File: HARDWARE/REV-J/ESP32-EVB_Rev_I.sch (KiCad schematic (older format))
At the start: 155 parts, among them CON1 TB3 DG306-5.0-3P, CON2 TB3 DG306-5.0-3P, Q1 BC817-40(SOT23), Q2 BC817-40(SOT23), Q3 Q12MHz/20pF/30ppm/2P/HC-49SM(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, Q4 BC817-40(SOT23), Q5 BC817-40(SOT23), Q6 BC817, Q7 BC817-40(SOT23), U1 BL4054B-42TPRN(SOT23-5), U10 BAT54C(SOT23-3), U2 SY8089AAAC(SOT23-5), U3 ESP-WROOM-32, U4 LAN8710A-EZC(QFN32), U5 CH340T(SSOP20W), U6 MCP2562-E/SN(SOIC-8_150mil), U7 RPM7236-H8, U8 NCP303LSN27T1G(SOT-23-5), U9 BAT54C(SOT23-3)

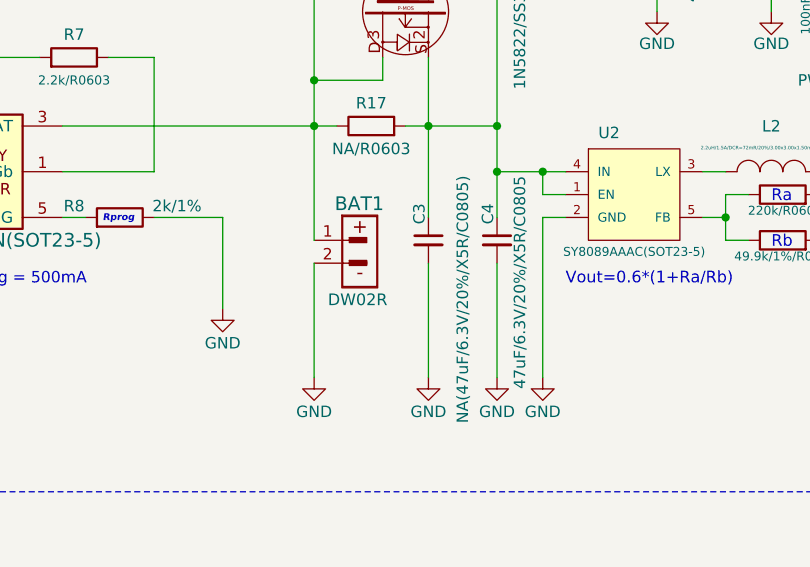
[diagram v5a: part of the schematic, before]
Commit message: re-position usb port+bat conector
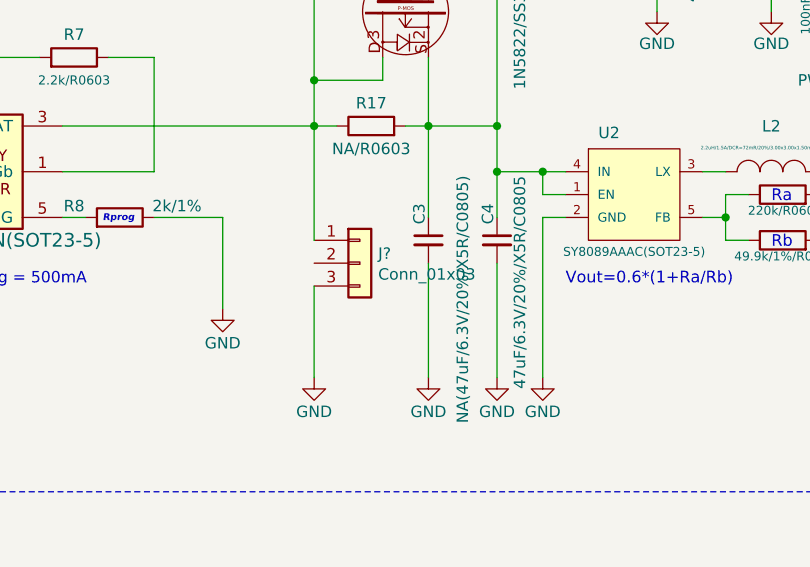
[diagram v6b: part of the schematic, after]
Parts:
- removed BAT1: DW02R, OLIMEX_Connectors-FP:LIPO_BAT-CON2DW02R, symbol ESP32-EVB_Rev_I:BAT_CON
- added J?: Conn_01x03, Connector_JST:JST_PH_B3B-PH-K_1x03_P2.00mm_Vertical, symbol Connector_Generic:Conn_01x03
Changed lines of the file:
@@
 Power Supply
 $Comp
-L ESP32-EVB_Rev_I:CON2 PWR2
-U 1 1 580E9D4F
-P 2400 2800
-F 0 "PWR2" H 2360 2960 60  0000 C CNN
-F 1 "NA(TB2 DG306-5.0-2P)" H 2300 2540 31  0000 C CNN
-F 2 "OLIMEX_Connectors-FP:TB2-DG306-5.0_2P" H 2325 2750 60  0001 C CNN
-F 3 "" H 2325 2750 60  0000 C CNN
-F 4 "Value 1" H 2400 2800 60  0001 C CNN "Fieldname 1"
-F 5 "Value2" H 2400 2800 60  0001 C CNN "Fieldname2"
-F 6 "Value3" H 2400 2800 60  0001 C CNN "Fieldname3"
-	1    2400 2800
-	1    0    0    -1
-$EndComp
-$Comp
 L ESP32-EVB_Rev_I:GND #PWR017
 U 1 1 580EB7F2
@@
 $EndComp
 $Comp
-L ESP32-EVB_Rev_I:BAT_CON BAT1
-U 1 1 581425A7
-P 6600 3450
-F 0 "BAT1" H 6490 3660 60  0000 L CNN
-F 1 "DW02R" H 6460 3240 51  0000 L CNN
-F 2 "OLIMEX_Connectors-FP:LIPO_BAT-CON2DW02R" H 6600 3450 60  0001 C CNN
-F 3 "" H 6600 3450 60  0000 C CNN
-F 4 "Value 1" H 6600 3450 60  0001 C CNN "Fieldname 1"
-F 5 "Value2" H 6600 3450 60  0001 C CNN "Fieldname2"
-F 6 "Value3" H 6600 3450 60  0001 C CNN "Fieldname3"
-	1    6600 3450
-	1    0    0    -1
-$EndComp
-$Comp
 L ESP32-EVB_Rev_I:GND #PWR031
 U 1 1 58142B69
@@
 Connection ~ 6900 1800
 Wire Wire Line
-	6400 4000 6400 3500
+	6400 4000 6400 3600
 Wire Wire Line
 	6400 2700 6400 2900
@@
 Wire Wire Line
 	11650 14400 12450 14400
+$Comp
+L ESP32-EVB_Rev_I:CON2 PWR2
+U 1 1 580E9D4F
+P 2400 2800
+F 0 "PWR2" H 2360 2960 60  0000 C CNN
+F 1 "NA(TB2 DG306-5.0-2P)" H 2300 2540 31  0000 C CNN
+F 2 "OLIMEX_Connectors-FP:TB2-DG306-5.0_2P" H 2325 2750 60  0001 C CNN
+F 3 "" H 2325 2750 60  0000 C CNN
+F 4 "Value 1" H 2400 2800 60  0001 C CNN "Fieldname 1"
+F 5 "Value2" H 2400 2800 60  0001 C CNN "Fieldname2"
+F 6 "Value3" H 2400 2800 60  0001 C CNN "Fieldname3"
+	1    2400 2800
+	1    0    0    -1
+$EndComp
+$Comp
+L Connector_Generic:Conn_01x03 J?
+U 1 1 6150B489
+P 6600 3500
+F 0 "J?" H 6680 3542 50  0000 L CNN
+F 1 "Conn_01x03" H 6680 3451 50  0000 L CNN
+F 2 "Connector_JST:JST_PH_B3B-PH-K_1x03_P2.00mm_Vertical" H 6600 3500 50  0001 C CNN
+F 3 "~" H 6600 3500 50  0001 C CNN
+	1    6600 3500
+	1    0    0    -1
+$EndComp
 $EndSCHEMATC
